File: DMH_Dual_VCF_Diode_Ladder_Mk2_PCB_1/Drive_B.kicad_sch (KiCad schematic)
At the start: 26 parts, among them J18 Conn_01x06_PinHeader, Q7 BC548, Q8 BC548, SW8 SW_DPDT_x2, U10 TL074

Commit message: Corrected pin header footprint assignments
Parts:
- J18: footprint (none) -> Connector_PinSocket_2.54mm:PinSocket_1x06_P2.54mm_Vertical
- J18: footprint Connector_PinHeader_2.54mm:PinHeader_1x10_P2.54mm_Vertical -> Connector_PinSocket_2.54mm:PinSocket_1x06_P2.54mm_Vertical
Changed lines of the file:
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@@
 			)
 		)
-		(property "Footprint" ""
+		(property "Footprint" "Connector_PinSocket_2.54mm:PinSocket_1x06_P2.54mm_Vertical"
 			(at 170.18 132.08 0)
 			(effects
@@
 			)
 		)
-		(property "Footprint" ""
+		(property "Footprint" "Connector_PinSocket_2.54mm:PinSocket_1x06_P2.54mm_Vertical"
 			(at 165.1 113.03 0)
 			(effects
@@
 			)
 		)
-		(property "Footprint" "Connector_PinHeader_2.54mm:PinHeader_1x10_P2.54mm_Vertical"
+		(property "Footprint" "Connector_PinSocket_2.54mm:PinSocket_1x06_P2.54mm_Vertical"
 			(at 110.49 129.54 0)
 			(effects
@@
 			)
 		)
-		(property "Footprint" "Connector_PinHeader_2.54mm:PinHeader_1x10_P2.54mm_Vertical"
+		(property "Footprint" "Connector_PinSocket_2.54mm:PinSocket_1x06_P2.54mm_Vertical"
 			(at 76.2 100.33 0)
 			(effects
@@
 			)
 		)
-		(property "Footprint" ""
+		(property "Footprint" "Connector_PinSocket_2.54mm:PinSocket_1x06_P2.54mm_Vertical"
 			(at 185.42 132.08 0)
 			(effects
@@
 			)
 		)
-		(property "Footprint" "Connector_PinHeader_2.54mm:PinHeader_1x10_P2.54mm_Vertical"
+		(property "Footprint" "Connector_PinSocket_2.54mm:PinSocket_1x06_P2.54mm_Vertical"
 			(at 63.5 81.28 0)
 			(effects

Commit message: PCB1 component placement in progress
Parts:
- J18: footprint Connector_PinSocket_2.54mm:PinSocket_1x06_P2.54mm_Vertical -> Connector_PinHeader_2.54mm:PinHeader_1x06_P2.54mm_Vertical
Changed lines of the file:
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@@
 			)
 		)
-		(property "Footprint" "Connector_PinSocket_2.54mm:PinSocket_1x06_P2.54mm_Vertical"
+		(property "Footprint" "Connector_PinHeader_2.54mm:PinHeader_1x06_P2.54mm_Vertical"
 			(at 170.18 132.08 0)
 			(effects
@@
 			)
 		)
-		(property "Footprint" "Connector_PinSocket_2.54mm:PinSocket_1x06_P2.54mm_Vertical"
+		(property "Footprint" "Connector_PinHeader_2.54mm:PinHeader_1x06_P2.54mm_Vertical"
 			(at 165.1 113.03 0)
 			(effects
@@
 			)
 		)
-		(property "Footprint" "Connector_PinSocket_2.54mm:PinSocket_1x06_P2.54mm_Vertical"
+		(property "Footprint" "Connector_PinHeader_2.54mm:PinHeader_1x06_P2.54mm_Vertical"
 			(at 110.49 129.54 0)
 			(effects
@@
 			)
 		)
-		(property "Footprint" "Connector_PinSocket_2.54mm:PinSocket_1x06_P2.54mm_Vertical"
+		(property "Footprint" "Connector_PinHeader_2.54mm:PinHeader_1x06_P2.54mm_Vertical"
 			(at 76.2 100.33 0)
 			(effects
@@
 			)
 		)
-		(property "Footprint" "Connector_PinSocket_2.54mm:PinSocket_1x06_P2.54mm_Vertical"
+		(property "Footprint" "Connector_PinHeader_2.54mm:PinHeader_1x06_P2.54mm_Vertical"
 			(at 185.42 132.08 0)
 			(effects
@@
 			)
 		)
-		(property "Footprint" "Connector_PinSocket_2.54mm:PinSocket_1x06_P2.54mm_Vertical"
+		(property "Footprint" "Connector_PinHeader_2.54mm:PinHeader_1x06_P2.54mm_Vertical"
 			(at 63.5 81.28 0)
 			(effects

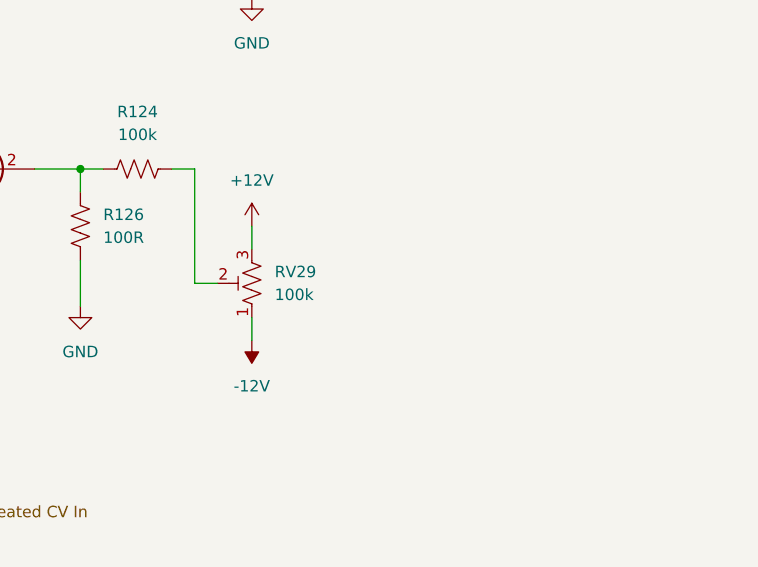
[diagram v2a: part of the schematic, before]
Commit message: Added trim pot functions to silkscreen
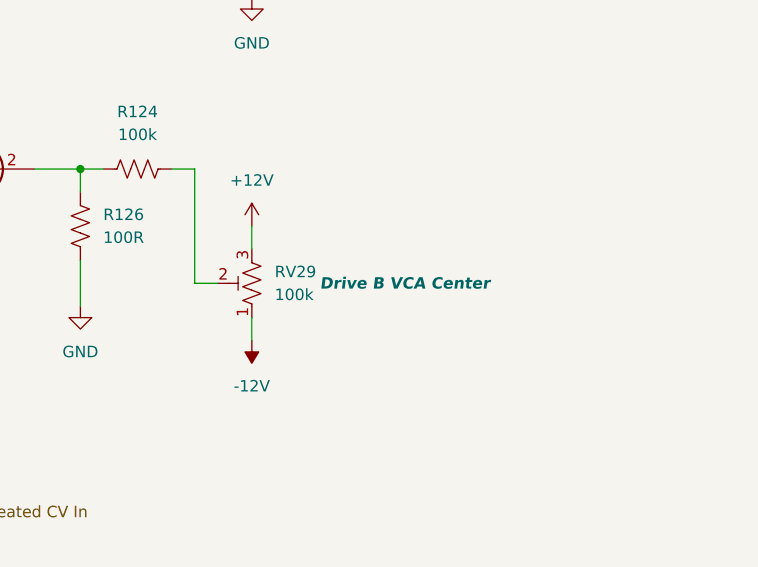
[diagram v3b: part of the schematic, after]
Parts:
- RV29: Function (none) -> Drive B VCA Center
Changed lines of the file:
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@@
 		(on_board yes)
 		(dnp no)
-		(fields_autoplaced yes)
 		(property "Reference" "RV29"
 			(at 224.79 100.3299 0)
@@
 			)
 		)
+		(property "Function" "Drive B VCA Center"
+			(at 239.268 101.6 0)
+			(effects
+				(font
+					(size 1.27 1.27)
+					(thickness 0.254)
+					(bold yes)
+					(italic yes)
+				)
+			)
+		)

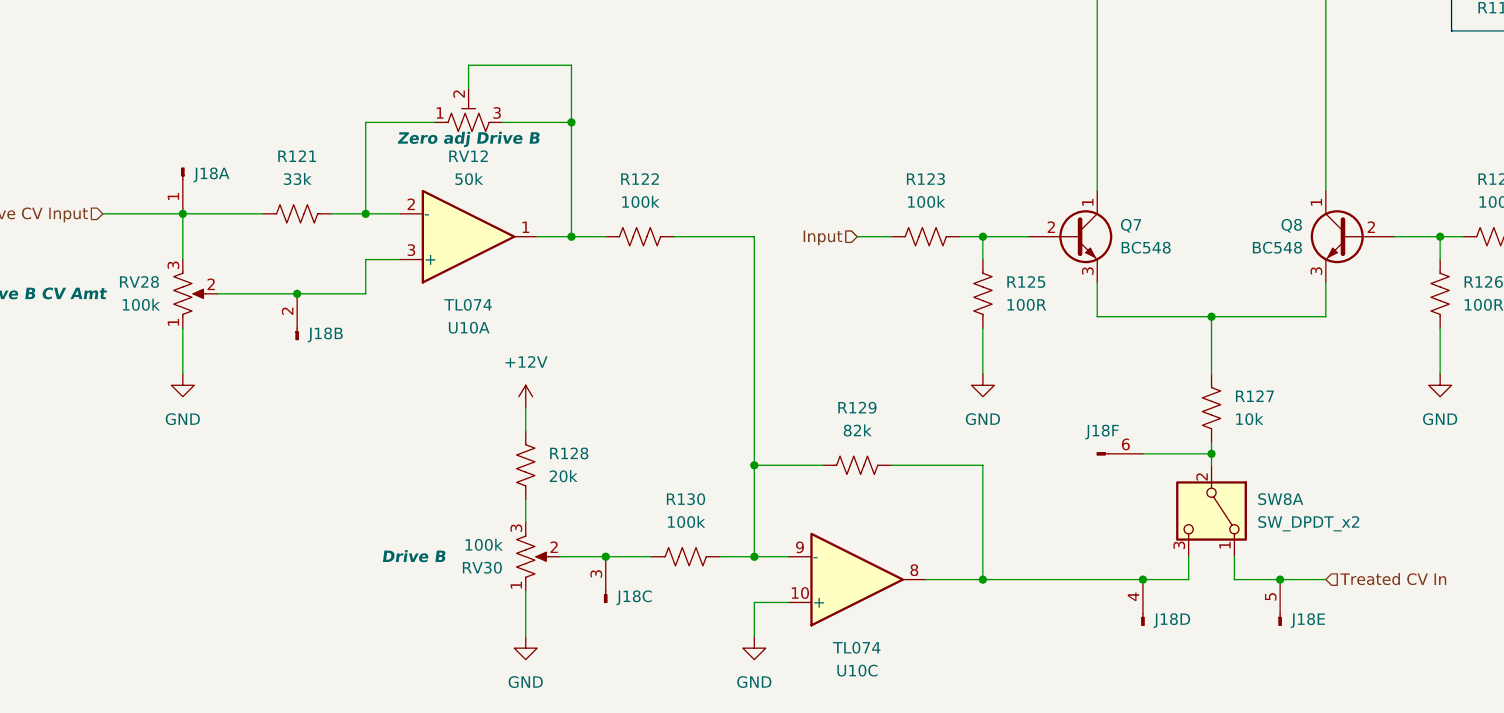
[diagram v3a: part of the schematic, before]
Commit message: Adjusted pin header connections
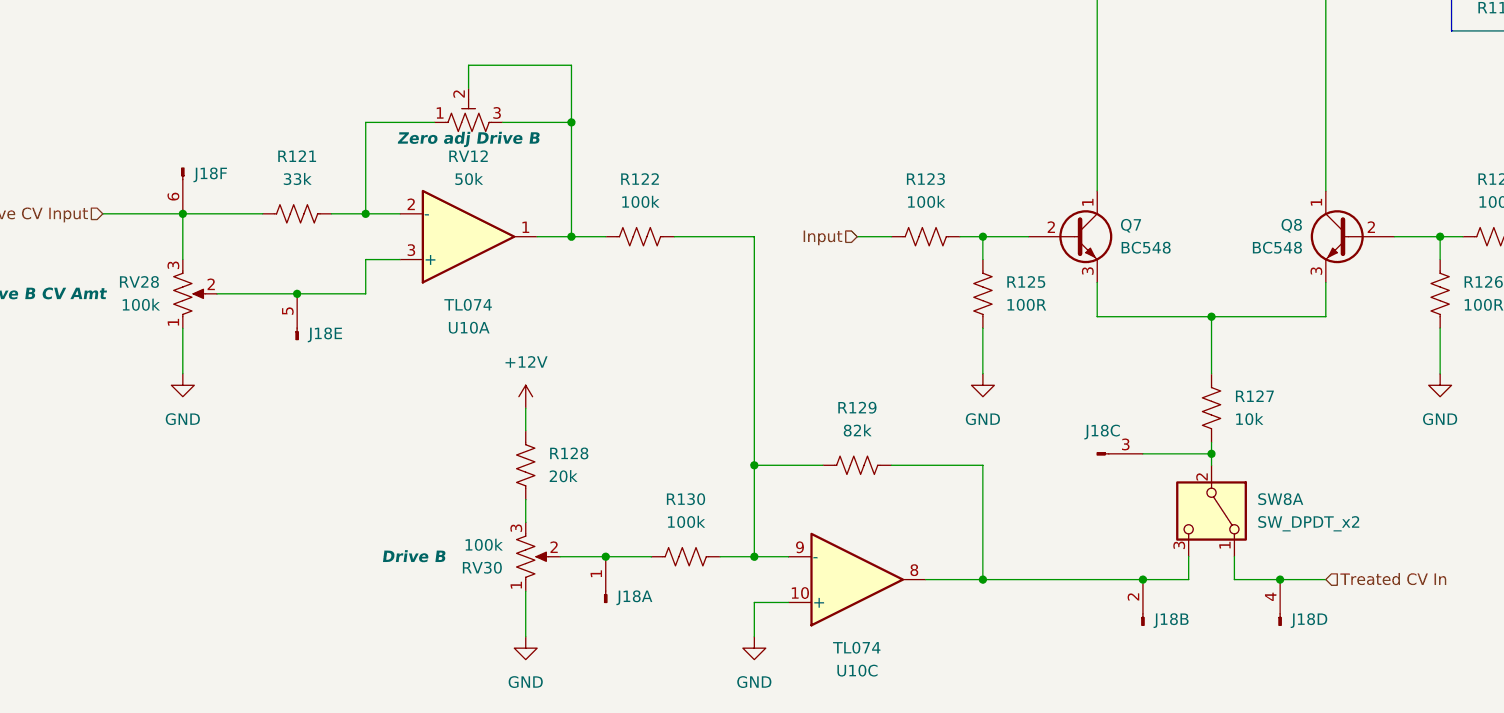
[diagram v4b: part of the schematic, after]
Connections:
- net Drive CV Input: now also J18.6 (Pin_6); no longer J18.1 (Pin_1)
- net Treated CV In: now also J18.4 (Pin_4); no longer J18.5 (Pin_5)
- net at R130.1, RV30.2: now also J18.1 (Pin_1); no longer J18.3 (Pin_3)
- net at R127.1, SW8.2 (B): now also J18.3 (Pin_3); no longer J18.6 (Pin_6)
- net at R129.2, SW8.3 (C), U10.8: now also J18.2 (Pin_2); no longer J18.4 (Pin_4)
- net at RV28.2, U10.3 (+): now also J18.5 (Pin_5); no longer J18.2 (Pin_2)
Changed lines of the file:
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@@
 		(lib_id "SynthStuff:Conn_01x06_PinHeader")
 		(at 170.18 132.08 90)
-		(unit 4)
+		(unit 2)
 		(exclude_from_sim no)
 		(in_bom yes)
@@
 			)
 		)
+		(property "Function" ""
+			(at 170.18 132.08 0)
+			(effects
+				(font
+					(size 1.27 1.27)
+				)
+			)
+		)
 		(pin "4"
 		)
@@
 				(path "/58f4306d-5387-4983-bb08-41a2313fd315/fc37885e-257b-42ac-a311-5adb1094134c"
 					(reference "J18")
-					(unit 4)
+					(unit 2)
 				)
 			)
@@
 		(lib_id "SynthStuff:Conn_01x06_PinHeader")
 		(at 165.1 113.03 0)
-		(unit 6)
+		(unit 3)
 		(exclude_from_sim no)
 		(in_bom yes)
@@
 			)
 		)
+		(property "Function" ""
+			(at 165.1 113.03 0)
+			(effects
+				(font
+					(size 1.27 1.27)
+				)
+			)
+		)
 		(pin "4"
 		)
@@
 				(path "/58f4306d-5387-4983-bb08-41a2313fd315/fc37885e-257b-42ac-a311-5adb1094134c"
 					(reference "J18")
-					(unit 6)
+					(unit 3)
 				)
 			)
@@
 		(lib_id "SynthStuff:Conn_01x06_PinHeader")
 		(at 110.49 129.54 90)
-		(unit 3)
+		(unit 1)
 		(exclude_from_sim no)
 		(in_bom yes)
@@
 				(path "/58f4306d-5387-4983-bb08-41a2313fd315/fc37885e-257b-42ac-a311-5adb1094134c"
 					(reference "J18")
-					(unit 3)
+					(unit 1)
 				)
 			)
@@
 		(lib_id "SynthStuff:Conn_01x06_PinHeader")
 		(at 76.2 100.33 90)
-		(unit 2)
+		(unit 5)
 		(exclude_from_sim no)
 		(in_bom yes)
@@
 				(path "/58f4306d-5387-4983-bb08-41a2313fd315/fc37885e-257b-42ac-a311-5adb1094134c"
 					(reference "J18")
-					(unit 2)
+					(unit 5)
 				)
 			)
@@
 		(lib_id "SynthStuff:Conn_01x06_PinHeader")
 		(at 185.42 132.08 90)
-		(unit 5)
+		(unit 4)
 		(exclude_from_sim no)
 		(in_bom yes)
@@
 			)
 		)
+		(property "Function" ""
+			(at 185.42 132.08 0)
+			(effects
+				(font
+					(size 1.27 1.27)
+				)
+			)
+		)
 		(pin "4"
 		)
@@
 				(path "/58f4306d-5387-4983-bb08-41a2313fd315/fc37885e-257b-42ac-a311-5adb1094134c"
 					(reference "J18")
-					(unit 5)
+					(unit 4)
 				)
 			)
@@
 		(lib_id "SynthStuff:Conn_01x06_PinHeader")
 		(at 63.5 81.28 270)
-		(unit 1)
+		(unit 6)
 		(exclude_from_sim no)
 		(in_bom yes)
@@
 				(path "/58f4306d-5387-4983-bb08-41a2313fd315/fc37885e-257b-42ac-a311-5adb1094134c"
 					(reference "J18")
-					(unit 1)
-				)
-			)
+					(unit 6)
+				)
+			)

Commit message: Changed VCA CV summing stage feedback to 100k
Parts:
- R129: value 82k -> 100k
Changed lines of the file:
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@@
 			)
 		)
-		(property "Value" "82k"
+		(property "Value" "100k"
 			(at 138.43 110.49 90)
 			(effects

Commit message: Updated various resistor values
... and deleted all VCAs output 1k resistors
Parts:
- removed R118: 1k, Resistor_THT:R_Axial_DIN0207_L6.3mm_D2.5mm_P7.62mm_Horizontal, symbol Device:R_US
- R128: value 20k -> 10k
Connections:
- net Output: now also R116.1, U10.7
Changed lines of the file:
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@@
 	(wire
 		(pts
-			(xy 257.81 50.8) (xy 266.7 50.8)
-		)
-		(stroke
-			(width 0)
-			(type default)
-		)
-	)
-	(wire
-		(pts
 			(xy 101.6 107.95) (xy 101.6 110.49)
 		)
@@
 	(wire
 		(pts
-			(xy 246.38 50.8) (xy 250.19 50.8)
+			(xy 246.38 50.8) (xy 266.7 50.8)
 		)
 		(stroke
@@
 			)
 		)
-		(property "Value" "20k"
+		(property "Value" "10k"
 			(at 104.14 115.5699 0)
 			(effects
@@
 					(unit 1)
 				)
-			)
-		)
-	)
-	(symbol
-		(lib_id "Device:R_US")
-		(at 254 50.8 270)
-		(unit 1)
-		(exclude_from_sim no)
-		(in_bom yes)
-		(on_board yes)
-		(dnp no)
-		(fields_autoplaced yes)
-		(property "Reference" "R118"
-			(at 254 44.45 90)
-			(effects
-				(font
-					(size 1.27 1.27)
-				)
-			)
-		)
-		(property "Value" "1k"
-			(at 254 46.99 90)
-			(effects
-				(font
-					(size 1.27 1.27)
-				)
-			)
-		)
-		(property "Footprint" "Resistor_THT:R_Axial_DIN0207_L6.3mm_D2.5mm_P7.62mm_Horizontal"
-			(at 253.746 51.816 90)
-			(effects
-				(font
-					(size 1.27 1.27)
-				)
-				(hide yes)
-			)
-		)
-		(property "Datasheet" "~"
-			(at 254 50.8 0)
-			(effects
-				(font
-					(size 1.27 1.27)
-				)
-				(hide yes)
-			)
-		)
-		(property "Description" "Resistor, US symbol"
-			(at 254 50.8 0)
-			(effects
-				(font
-					(size 1.27 1.27)
-				)
-				(hide yes)
-			)
-		)
-		(property "Function" ""
-			(at 254 50.8 0)
-			(effects
-				(font
-					(size 1.27 1.27)
-				)
-			)
-		)
-		(pin "1"
-		)
-		(pin "2"
-		)
-		(instances
-			(project "DMH_Dual_VCF_Diode_Ladder_Mk2_PCB_1"
-				(path "/58f4306d-5387-4983-bb08-41a2313fd315/fc37885e-257b-42ac-a311-5adb1094134c"
-					(reference "R118")
-					(unit 1)
-				)
